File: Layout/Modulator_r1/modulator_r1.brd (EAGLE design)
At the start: 75.2 x 49.5 mm, 92 parts, among them Q1 FA-20H, U1 ATMEGA328P-AU, U2 TPS79933QDDCRQ1, U3 CC1125RHBT, U4 MCP1700T-3302E/TT, U5 FT232RL, U6 SIP32509DT-T1-GE3

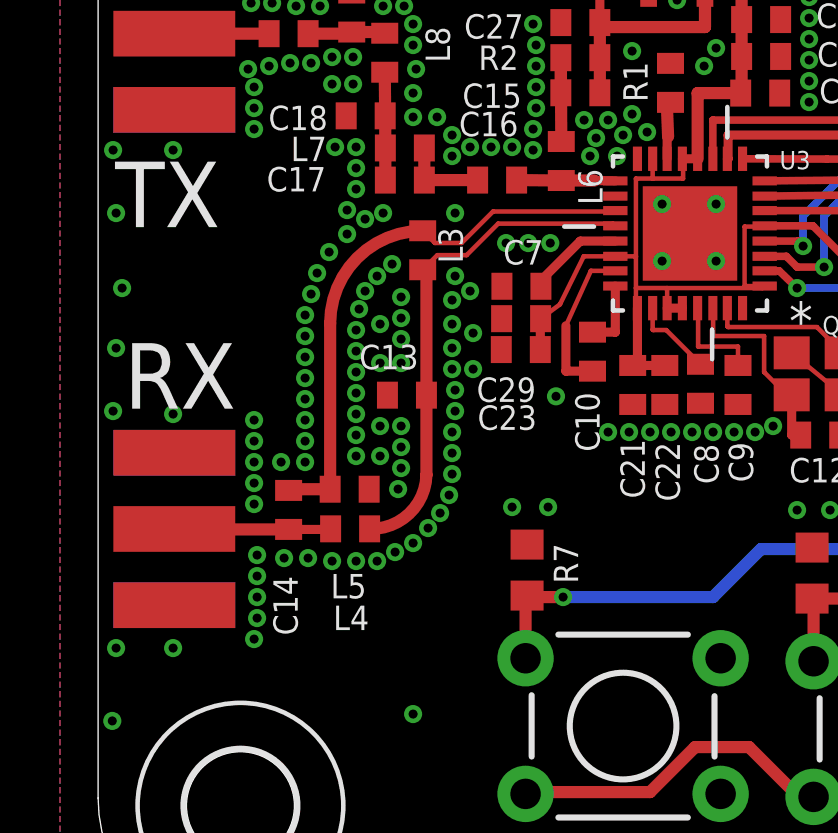
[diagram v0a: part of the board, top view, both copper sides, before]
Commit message: Redo RX layout to better match TI Reference.
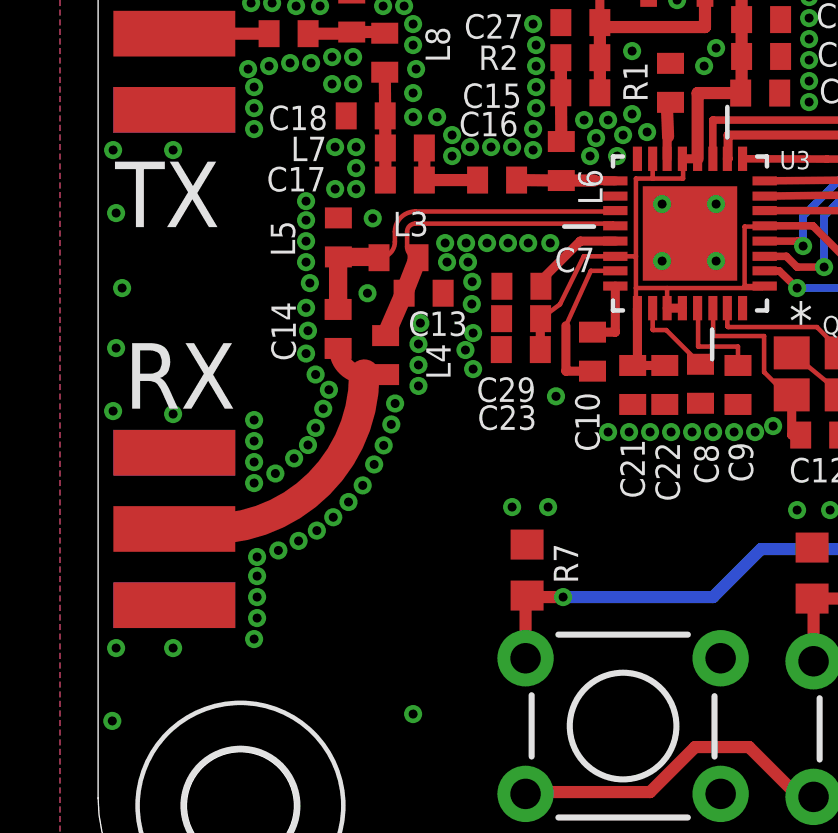
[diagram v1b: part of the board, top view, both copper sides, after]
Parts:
- moved L5 8.40 mm to (8.01, 23.7), turned to 90 degrees
- moved C14 6.25 mm to (8.00, 20.6)
- moved L4 5.91 mm to (9.58, 19.8), turned to 270 degrees
- moved C13 3.44 mm to (10.9, 21.8), turned to 180 degrees
- moved L3 0.84 mm to (10.0, 23.0), turned to 180 degrees
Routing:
- net CC_LNA_P: track 18.3 -> 11.8 mm
- net CC_LNA_N: track 16.6 -> 10.9 mm
- net N$17: track 5.46 -> 10.4 mm
- net GND: vias 326 -> 304

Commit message: Complete LDO circuit.
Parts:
- added C35: 10nF, resistor:C0603
- moved 3V3_RF 2.90 mm to (12.5, 32.6)
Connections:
- new net N$30: C35.1, U2.4
- net GND: now also C35.2
- net VCC_LOGIC: now also U2.3
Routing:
- net N$30: track 0.00 -> 2.28 mm
- net CC_VDD: track 51.0 -> 52.8 mm
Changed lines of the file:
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@@
 <attribute name="SUPPLIER" value="Texas Instruments" x="19.29" y="33.33" size="1.524" layer="27" font="fixed" rot="R270" display="off"/>
 <attribute name="OC_FARNELL" value="-" x="19.29" y="33.33" size="1.524" layer="27" font="fixed" rot="R270" display="off"/>
-<attribute name="NAME" x="16.73" y="33.8844" size="0.8128" layer="25" ratio="10" rot="SR270"/>
+<attribute name="NAME" x="21.1115" y="33.9479" size="0.8128" layer="25" ratio="10" rot="SR270"/>
 </element>
 <element name="LED1" library="led" package="CHIPLED_1206" value="" x="59.42" y="15.59" smashed="yes" rot="R270">
@@
 </element>
 <element name="C19" library="resistor" package="C0402" value="6p2" x="8.455" y="31.185" smashed="yes" rot="R90">
-<attribute name="NAME" x="8.833" y="32.75" size="0.8128" layer="25" rot="R90"/>
+<attribute name="NAME" x="8.833" y="32.623" size="0.8128" layer="25" rot="R90"/>
 </element>
 <element name="L6" library="resistor" package="R0402" value="56n" x="15.44" y="26.235" smashed="yes" rot="R270">
@@
 <attribute name="VALUE" x="43.33" y="14.903" size="0.0254" layer="27"/>
 </element>
-<element name="3V3_RF" library="testpad" package="B2,54" value="PTR1B2,54" x="15.1" y="33.9" smashed="yes">
-<attribute name="TP_SIGNAL_NAME" value="" x="13.83" y="30.725" size="1" layer="37"/>
-<attribute name="NAME" x="9.53" y="35.451" size="1.27" layer="25" ratio="10"/>
-<attribute name="VALUE" x="13.83" y="32.503" size="0.0254" layer="27"/>
+<element name="3V3_RF" library="testpad" package="B2,54" value="PTR1B2,54" x="12.4965" y="32.63" smashed="yes">
+<attribute name="TP_SIGNAL_NAME" value="" x="11.2265" y="29.455" size="1" layer="37"/>
+<attribute name="NAME" x="9.149" y="34.689" size="1.27" layer="25" ratio="10"/>
+<attribute name="VALUE" x="11.2265" y="31.233" size="0.0254" layer="27"/>
 </element>
 <element name="GND" library="testpad" package="B2,54" value="PTR1B2,54" x="71.3" y="11.6">
@@
 <element name="C34" library="resistor" package="C0603" value="100nF" x="52.6415" y="29.6545" smashed="yes" rot="R270">
 <attribute name="NAME" x="53.975" y="29.845" size="0.8128" layer="25" rot="R270"/>
+</element>
+<element name="C35" library="resistor" package="C0603" value="10nF" x="16.7005" y="34.417" smashed="yes" rot="R90">
+<attribute name="NAME" x="15.9385" y="32.4485" size="0.8128" layer="25" rot="R90"/>
 </element>
 </elements>
@@
 <via x="20.2" y="29.4" extent="1-16" drill="0.3"/>
 <via x="17.5" y="27.1" extent="1-16" drill="0.3"/>
-<via x="19.3" y="35.8" extent="1-16" drill="0.3"/>
+<via x="19.3" y="32.4345" extent="1-16" drill="0.3"/>
 <via x="19.3" y="31.6" extent="1-16" drill="0.3"/>
 <via x="0.8" y="22" extent="1-16" drill="0.3"/>
@@
 <via x="19.3" y="33.3" extent="1-16" drill="0.3"/>
 <via x="20.2" y="33.3" extent="1-16" drill="0.3"/>
-<via x="15" y="32" extent="1-16" drill="0.3"/>
-<via x="15.7" y="32" extent="1-16" drill="0.3"/>
-<via x="17.2" y="36.2" extent="1-16" drill="0.3"/>
+<via x="14.8095" y="31.9365" extent="1-16" drill="0.3"/>
+<via x="15.5095" y="31.9365" extent="1-16" drill="0.3"/>
+<via x="17.1365" y="36.454" extent="1-16" drill="0.3"/>
 <via x="17.2" y="37.2" extent="1-16" drill="0.3"/>
-<via x="16.5" y="36.7" extent="1-16" drill="0.3"/>
+<via x="16.3095" y="36.446" extent="1-16" drill="0.3"/>
 <via x="12.5" y="20.5" extent="1-16" drill="0.3"/>
 <via x="12.5" y="19.3" extent="1-16" drill="0.3"/>
@@
 <contactref element="GND" pad="TP"/>
 <via x="8.979" y="21.8285" extent="1-16" drill="0.3"/>
-<wire x1="20.6" y1="22.9" x2="19.73" y2="23.82" width="0" layer="19" extent="1-1"/>
-<wire x1="64.085" y1="27.055" x2="65.5" y2="26.9" width="0" layer="19" extent="1-1"/>
 <via x="9.2015" y="16.121" extent="1-16" drill="0.3"/>
 <via x="9.519" y="16.756" extent="1-16" drill="0.3"/>
@@
 <via x="7.9015" y="25.3" extent="1-16" drill="0.3"/>
 <via x="12.33" y="22.865" extent="1-16" drill="0.3"/>
+<contactref element="C35" pad="2"/>
+<wire x1="20.6" y1="22.9" x2="19.73" y2="23.82" width="0" layer="19" extent="1-1"/>
+<wire x1="64.085" y1="27.055" x2="65.5" y2="26.9" width="0" layer="19" extent="1-1"/>
 </signal>
 <signal name="VCCIO">
@@
 <wire x1="22.2192" y1="24.05" x2="22.2192" y2="24.074" width="0.15" layer="1"/>
 <contactref element="3V3_RF" pad="TP"/>
-<wire x1="15.1" y1="33.9" x2="16.725" y2="32.275" width="0.3048" layer="1"/>
-<wire x1="16.725" y1="32.275" x2="16.725" y2="30.85" width="0.3048" layer="1"/>
 <wire x1="17.9774" y1="21.3308" x2="17.9774" y2="19.42" width="0.3048" layer="1"/>
 <wire x1="17.9774" y1="19.42" x2="17.82" y2="19.42" width="0.3048" layer="1"/>
@@
 <wire x1="14.75" y1="20.98" x2="14.74" y2="20.97" width="0.3048" layer="1"/>
 <wire x1="14.74" y1="20.97" x2="14.74" y2="19.95" width="0.3048" layer="1"/>
+<wire x1="16.725" y1="30.85" x2="16.725" y2="31.7255" width="0.3048" layer="1"/>
+<wire x1="16.725" y1="31.7255" x2="15.8115" y2="32.639" width="0.3048" layer="1"/>
+<wire x1="15.8115" y1="32.639" x2="12.5055" y2="32.639" width="0.3048" layer="1"/>
+<wire x1="12.5055" y1="32.639" x2="12.4965" y2="32.63" width="0.3048" layer="1"/>
 </signal>
 <signal name="N$8">
@@
 <wire x1="53.46" y1="33.97" x2="53.46" y2="36.06" width="0.4064" layer="1"/>
 <wire x1="53.46" y1="36.06" x2="55.4" y2="38" width="0.4064" layer="1"/>
+<contactref element="U2" pad="3"/>
+<wire x1="18.3502" y1="34.6254" x2="20.2298" y2="34.6254" width="0" layer="19" extent="1-1"/>
 </signal>
 <signal name="N$22">
@@
 <wire x1="53.4425" y1="28.8045" x2="52.6415" y2="28.8045" width="0.4064" layer="1"/>
 </signal>
+<signal name="N$30">
+<contactref element="C35" pad="1"/>
+<contactref element="U2" pad="4"/>
+<wire x1="16.7005" y1="33.567" x2="18.2329" y2="32.0346" width="0.4064" layer="1"/>
+<wire x1="18.2329" y1="32.0346" x2="18.3502" y2="32.0346" width="0.4064" layer="1"/>
+</signal>
 </signals>

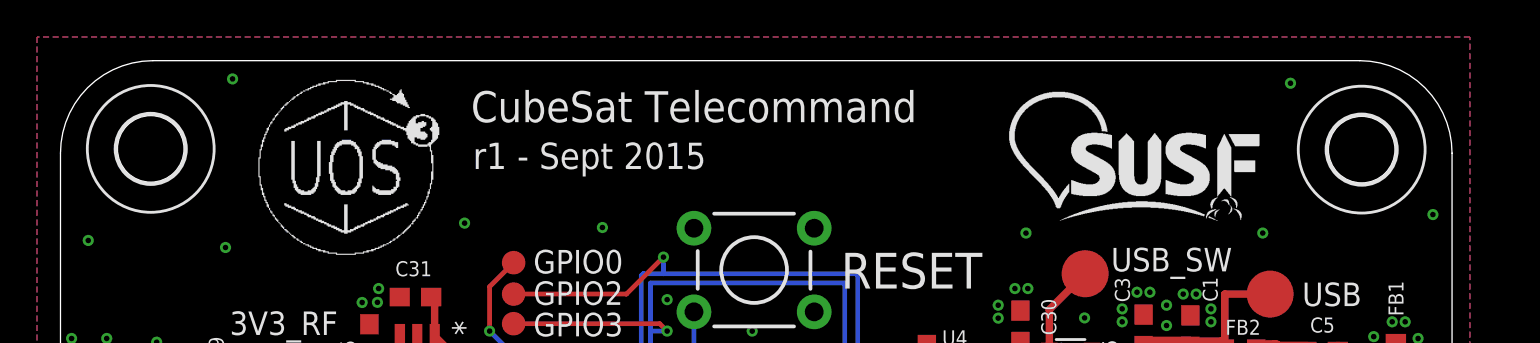
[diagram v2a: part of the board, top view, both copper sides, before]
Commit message: Actually line up mounting holes.
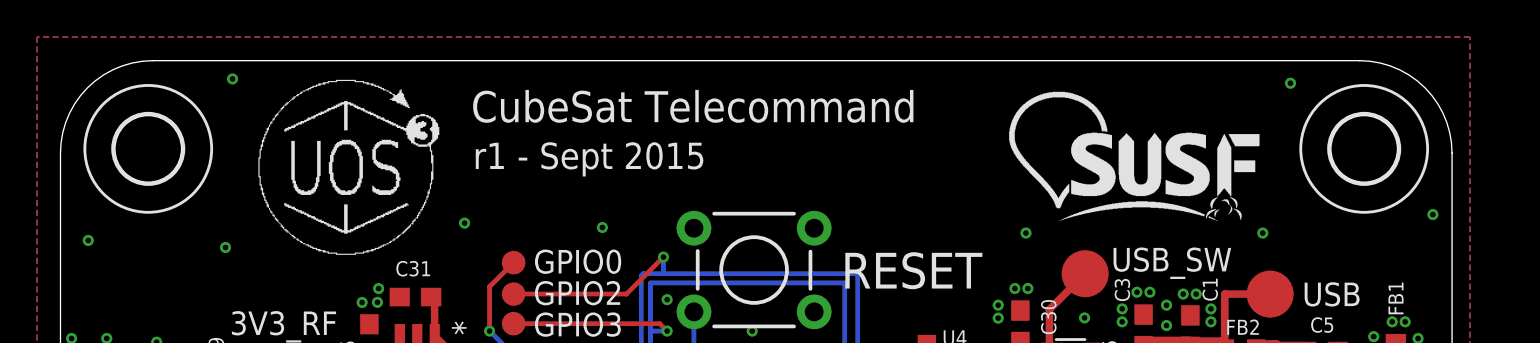
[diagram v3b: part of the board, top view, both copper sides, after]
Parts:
- moved U$4 0.14 mm to (70.5, 44.8)
- moved U$5 0.13 mm to (4.75, 44.8)
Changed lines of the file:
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@@
 <element name="U$2" library="holes" package="3,6" value="" x="4.745" y="4.745"/>
 <element name="U$3" library="holes" package="3,6" value="" x="70.485" y="4.745"/>
-<element name="U$4" library="holes" package="3,6" value="" x="70.35" y="44.71"/>
-<element name="U$5" library="holes" package="3,6" value="" x="4.88" y="44.75"/>
+<element name="U$4" library="holes" package="3,6" value="" x="70.485" y="44.75"/>
+<element name="U$5" library="holes" package="3,6" value="" x="4.745" y="44.75"/>
 <element name="U2" library="Texas Instruments_By_element14_Batch_1" package="SOT95P280X110-5N" value="TPS79933QDDCRQ1" x="19.29" y="33.33" smashed="yes" rot="R270">
 <attribute name="PACKAGE" value="SOT-5" x="19.29" y="33.33" size="1.524" layer="27" font="fixed" rot="R270" display="off"/>
